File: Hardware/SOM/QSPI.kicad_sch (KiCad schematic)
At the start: 1 part, among them U4 W25Q128JVP

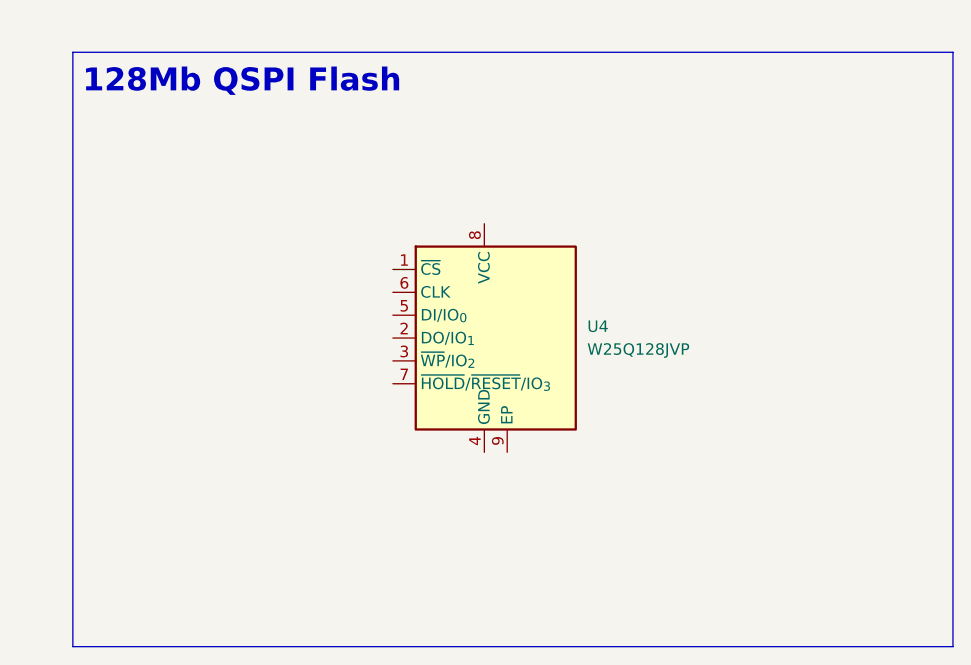
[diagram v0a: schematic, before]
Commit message: QSPI, banks IO decoupling
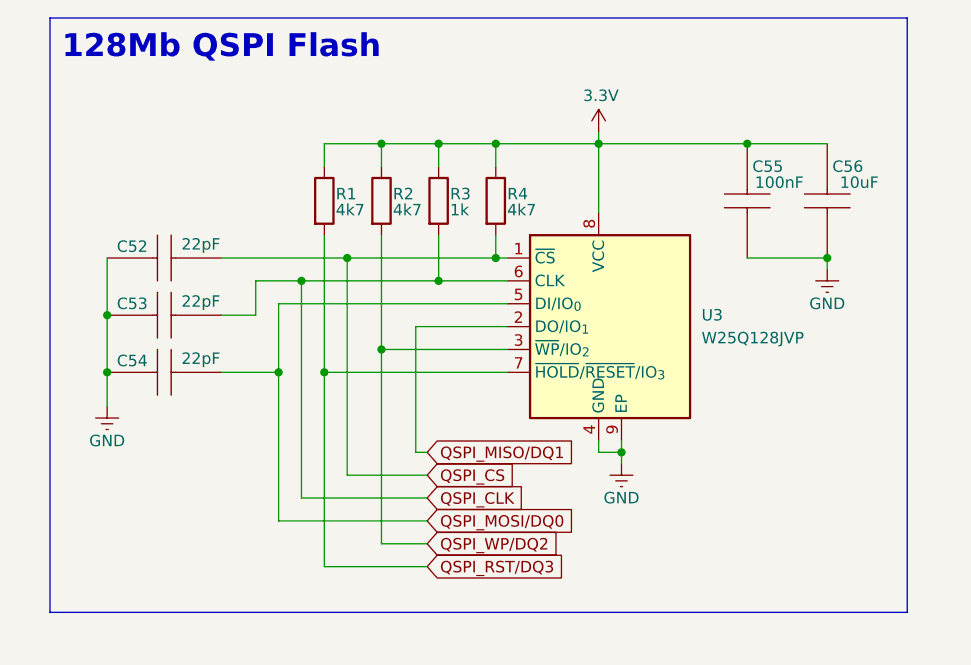
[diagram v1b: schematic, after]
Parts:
- added C52, C53, C54: 22pF, Capacitor_SMD:C_0402_1005Metric, symbol RA8M1:885012205092
- added C55: 100nF, Capacitor_SMD:C_0402_1005Metric, symbol RA8M1:885012205092
- added C56: 10uF, Capacitor_SMD:C_0402_1005Metric, symbol RA8M1:885012205092
- added R1, R2, R4: 4k7, Resistor_SMD:R_0402_1005Metric, symbol Device:R
- added R3: 1k, Resistor_SMD:R_0402_1005Metric, symbol Device:R
- renumbered U4 to U3
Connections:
- net QSPI_CS: now reaches U3.1 (~{CS})
- net QSPI_CS: now also C52.1, R4.2
- net QSPI_MISO/DQ1: now reaches U3.2 (DO/IO_{1})
- net QSPI_WP/DQ2: now reaches U3.3 (~{WP}/IO_{2})
- net QSPI_WP/DQ2: now also R2.2
- net GND: now reaches U3.4 (GND)
- net GND: now also U3.9 (EP), C52.2, C53.2, C54.2, C55.1, C56.1
- net QSPI_MOSI/DQ0: now reaches U3.5 (DI/IO_{0})
- net QSPI_MOSI/DQ0: now also C54.1
- net QSPI_CLK: now reaches U3.6 (CLK)
- net QSPI_CLK: now also C53.1, R3.2
- net QSPI_RST/DQ3: now reaches U3.7 (~{HOLD}/~{RESET}/IO_{3})
- net QSPI_RST/DQ3: now also R1.2
- net 3.3V: now reaches U3.8 (VCC)
- net 3.3V: now also C55.2, C56.2, R1.1, R2.1, R3.1, R4.1
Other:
- moved on the sheet: U3

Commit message: QSPI connected
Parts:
- added R5: 0R, Resistor_SMD:R_0402_1005Metric, symbol Device:R
- added R6: 49.9R, Resistor_SMD:R_0402_1005Metric, symbol Device:R
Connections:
- net QSPI_CLK: now also R6.2; no longer C53.1, R3.2, U3.6 (CLK)
- net QSPI_CS: now also R5.2; no longer C52.1, R4.2, U3.1 (~{CS})
- new net: C53.1, R3.2, R6.1, U3.6 (CLK)
- new net: C52.1, R4.2, R5.1, U3.1 (~{CS})
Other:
- moved on the sheet: C52, C53, C54

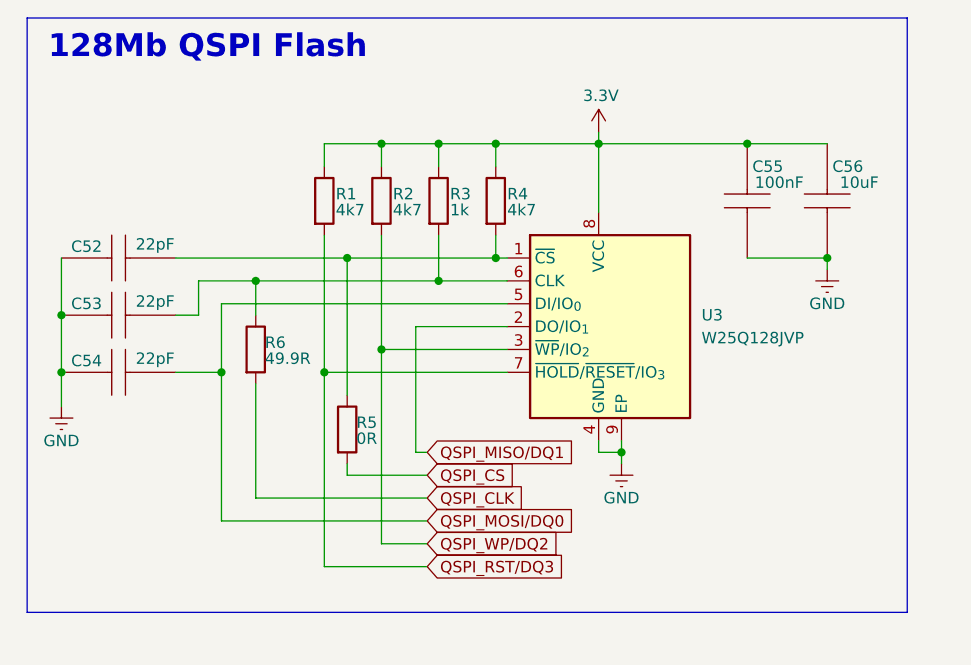
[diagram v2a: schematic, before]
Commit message: SOM: DDR pull-ups
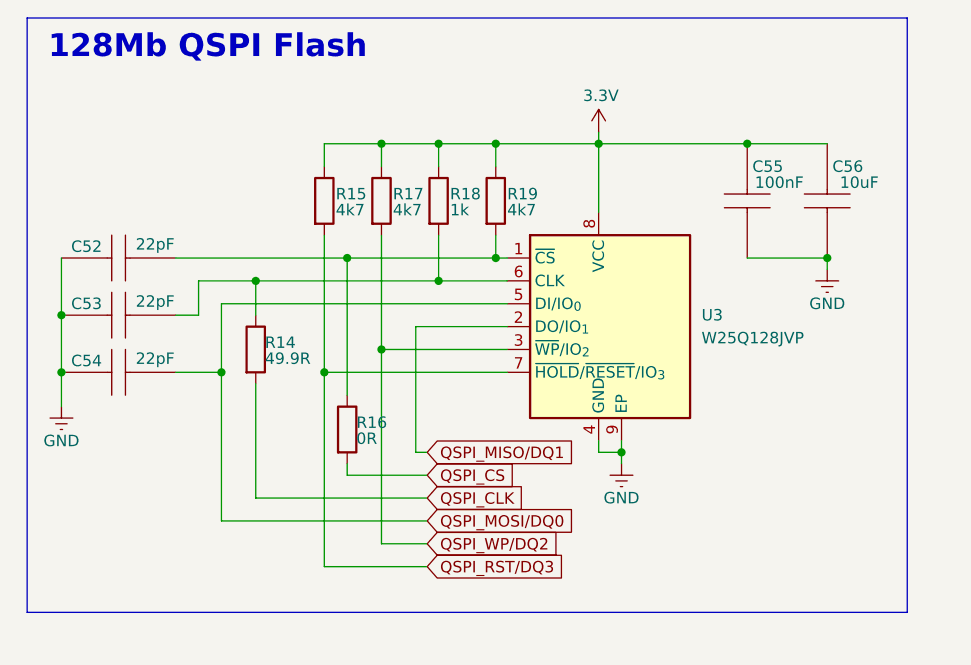
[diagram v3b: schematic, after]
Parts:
- renumbered R6 to R14, R1 to R15, R5 to R16, R2 to R17, R3 to R18, R4 to R19
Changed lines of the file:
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@@
 		(on_board yes)
 		(dnp no)
-		(property "Reference" "R2"
+		(property "Reference" "R17"
 			(at 137.16 84.328 0)
 			(effects
@@
 			(project "LFE5UM5G-85F_SOM"
 				(path "/de32abb0-ff3b-4c67-a91a-eed08140b1b2/2798ff7a-264e-45e9-a081-6e03072ed147"
-					(reference "R2")
+					(reference "R17")
 					(unit 1)
 				)
@@
 		(on_board yes)
 		(dnp no)
-		(property "Reference" "R6"
+		(property "Reference" "R14"
 			(at 122.936 100.838 0)
 			(effects
@@
 			(project "LFE5UM5G-85F_SOM"
 				(path "/de32abb0-ff3b-4c67-a91a-eed08140b1b2/2798ff7a-264e-45e9-a081-6e03072ed147"
-					(reference "R6")
+					(reference "R14")
 					(unit 1)
 				)
@@
 		(on_board yes)
 		(dnp no)
-		(property "Reference" "#PWR031"
+		(property "Reference" "#PWR038"
 			(at 160.02 81.28 0)
 			(effects
@@
 			(project "LFE5UM5G-85F_SOM"
 				(path "/de32abb0-ff3b-4c67-a91a-eed08140b1b2/2798ff7a-264e-45e9-a081-6e03072ed147"
-					(reference "#PWR031")
+					(reference "#PWR038")
 					(unit 1)
 				)
@@
 		(on_board yes)
 		(dnp no)
-		(property "Reference" "R5"
+		(property "Reference" "R16"
 			(at 133.096 109.728 0)
 			(effects
@@
 			(project "LFE5UM5G-85F_SOM"
 				(path "/de32abb0-ff3b-4c67-a91a-eed08140b1b2/2798ff7a-264e-45e9-a081-6e03072ed147"
-					(reference "R5")
+					(reference "R16")
 					(unit 1)
 				)
@@
 		(on_board yes)
 		(dnp no)
-		(property "Reference" "#PWR030"
+		(property "Reference" "#PWR037"
 			(at 100.33 114.3 0)
 			(effects
@@
 			(project "LFE5UM5G-85F_SOM"
 				(path "/de32abb0-ff3b-4c67-a91a-eed08140b1b2/2798ff7a-264e-45e9-a081-6e03072ed147"
-					(reference "#PWR030")
+					(reference "#PWR037")
 					(unit 1)
 				)
@@
 		(on_board yes)
 		(dnp no)
-		(property "Reference" "R1"
+		(property "Reference" "R15"
 			(at 130.81 84.328 0)
 			(effects
@@
 			(project "LFE5UM5G-85F_SOM"
 				(path "/de32abb0-ff3b-4c67-a91a-eed08140b1b2/2798ff7a-264e-45e9-a081-6e03072ed147"
-					(reference "R1")
+					(reference "R15")
 					(unit 1)
 				)
@@
 		(on_board yes)
 		(dnp no)
-		(property "Reference" "#PWR032"
+		(property "Reference" "#PWR039"
 			(at 162.56 120.65 0)
 			(effects
@@
 			(project "LFE5UM5G-85F_SOM"
 				(path "/de32abb0-ff3b-4c67-a91a-eed08140b1b2/2798ff7a-264e-45e9-a081-6e03072ed147"
-					(reference "#PWR032")
+					(reference "#PWR039")
 					(unit 1)
 				)
@@
 		(on_board yes)
 		(dnp no)
-		(property "Reference" "R3"
+		(property "Reference" "R18"
 			(at 143.51 84.328 0)
 			(effects
@@
 			(project "LFE5UM5G-85F_SOM"
 				(path "/de32abb0-ff3b-4c67-a91a-eed08140b1b2/2798ff7a-264e-45e9-a081-6e03072ed147"
-					(reference "R3")
+					(reference "R18")
 					(unit 1)
 				)
@@
 		(on_board yes)
 		(dnp no)
-		(property "Reference" "#PWR033"
+		(property "Reference" "#PWR040"
 			(at 185.42 99.06 0)
 			(effects
@@
 			(project "LFE5UM5G-85F_SOM"
 				(path "/de32abb0-ff3b-4c67-a91a-eed08140b1b2/2798ff7a-264e-45e9-a081-6e03072ed147"
-					(reference "#PWR033")
+					(reference "#PWR040")
 					(unit 1)
 				)
@@
 		(on_board yes)
 		(dnp no)
-		(property "Reference" "R4"
+		(property "Reference" "R19"
 			(at 149.86 84.328 0)
 			(effects
@@
 			(project "LFE5UM5G-85F_SOM"
 				(path "/de32abb0-ff3b-4c67-a91a-eed08140b1b2/2798ff7a-264e-45e9-a081-6e03072ed147"
-					(reference "R4")
-					(unit 1)
-				)
+					(reference "R19")
+					(unit 1)
+				)

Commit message: SOM: power supply update
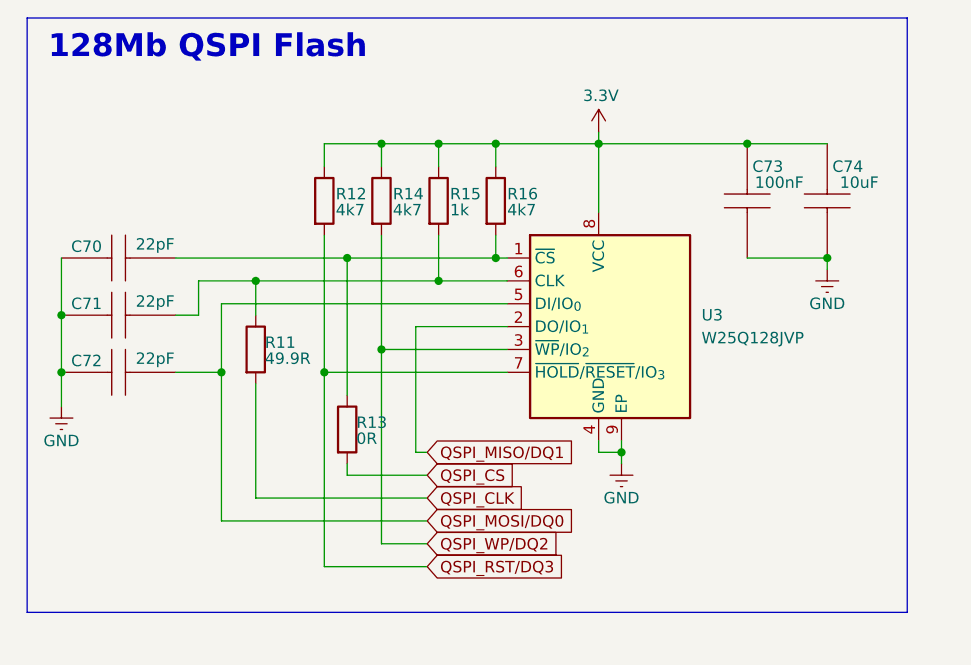
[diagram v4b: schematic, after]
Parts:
- renumbered C52 to C70, C53 to C71, C54 to C72, C55 to C73, C56 to C74, R14 to R11, R15 to R12, R16 to R13, R17 to R14, R18 to R15, R19 to R16
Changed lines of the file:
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@@
 		(on_board yes)
 		(dnp no)
-		(property "Reference" "R17"
+		(property "Reference" "R14"
 			(at 137.16 84.328 0)
 			(effects
@@
 			(project "LFE5UM5G-85F_SOM"
 				(path "/de32abb0-ff3b-4c67-a91a-eed08140b1b2/2798ff7a-264e-45e9-a081-6e03072ed147"
-					(reference "R17")
+					(reference "R14")
 					(unit 1)
 				)
@@
 		(on_board yes)
 		(dnp no)
-		(property "Reference" "R14"
+		(property "Reference" "R11"
 			(at 122.936 100.838 0)
 			(effects
@@
 			(project "LFE5UM5G-85F_SOM"
 				(path "/de32abb0-ff3b-4c67-a91a-eed08140b1b2/2798ff7a-264e-45e9-a081-6e03072ed147"
-					(reference "R14")
+					(reference "R11")
 					(unit 1)
 				)
@@
 		(on_board yes)
 		(dnp no)
-		(property "Reference" "#PWR038"
+		(property "Reference" "#PWR043"
 			(at 160.02 81.28 0)
 			(effects
@@
 			(project "LFE5UM5G-85F_SOM"
 				(path "/de32abb0-ff3b-4c67-a91a-eed08140b1b2/2798ff7a-264e-45e9-a081-6e03072ed147"
-					(reference "#PWR038")
+					(reference "#PWR043")
 					(unit 1)
 				)
@@
 		(on_board yes)
 		(dnp no)
-		(property "Reference" "R16"
+		(property "Reference" "R13"
 			(at 133.096 109.728 0)
 			(effects
@@
 			(project "LFE5UM5G-85F_SOM"
 				(path "/de32abb0-ff3b-4c67-a91a-eed08140b1b2/2798ff7a-264e-45e9-a081-6e03072ed147"
-					(reference "R16")
+					(reference "R13")
 					(unit 1)
 				)
@@
 		(on_board yes)
 		(dnp no)
-		(property "Reference" "C52"
+		(property "Reference" "C70"
 			(at 103.124 90.17 0)
 			(effects
@@
 			(project "LFE5UM5G-85F_SOM"
 				(path "/de32abb0-ff3b-4c67-a91a-eed08140b1b2/2798ff7a-264e-45e9-a081-6e03072ed147"
-					(reference "C52")
+					(reference "C70")
 					(unit 1)
 				)
@@
 		(on_board yes)
 		(dnp no)
-		(property "Reference" "#PWR037"
+		(property "Reference" "#PWR042"
 			(at 100.33 114.3 0)
 			(effects
@@
 			(project "LFE5UM5G-85F_SOM"
 				(path "/de32abb0-ff3b-4c67-a91a-eed08140b1b2/2798ff7a-264e-45e9-a081-6e03072ed147"
-					(reference "#PWR037")
+					(reference "#PWR042")
 					(unit 1)
 				)
@@
 		(on_board yes)
 		(dnp no)
-		(property "Reference" "C55"
+		(property "Reference" "C73"
 			(at 178.816 81.28 90)
 			(effects
@@
 			(project "LFE5UM5G-85F_SOM"
 				(path "/de32abb0-ff3b-4c67-a91a-eed08140b1b2/2798ff7a-264e-45e9-a081-6e03072ed147"
-					(reference "C55")
+					(reference "C73")
 					(unit 1)
 				)
@@
 		(on_board yes)
 		(dnp no)
-		(property "Reference" "C53"
+		(property "Reference" "C71"
 			(at 103.124 96.52 0)
 			(effects
@@
 			(project "LFE5UM5G-85F_SOM"
 				(path "/de32abb0-ff3b-4c67-a91a-eed08140b1b2/2798ff7a-264e-45e9-a081-6e03072ed147"
-					(reference "C53")
+					(reference "C71")
 					(unit 1)
 				)
@@
 		(on_board yes)
 		(dnp no)
-		(property "Reference" "C56"
+		(property "Reference" "C74"
 			(at 187.706 81.28 90)
 			(effects
@@
 			(project "LFE5UM5G-85F_SOM"
 				(path "/de32abb0-ff3b-4c67-a91a-eed08140b1b2/2798ff7a-264e-45e9-a081-6e03072ed147"
-					(reference "C56")
+					(reference "C74")
 					(unit 1)
 				)
@@
 		(on_board yes)
 		(dnp no)
-		(property "Reference" "R15"
+		(property "Reference" "R12"
 			(at 130.81 84.328 0)
 			(effects
@@
 			(project "LFE5UM5G-85F_SOM"
 				(path "/de32abb0-ff3b-4c67-a91a-eed08140b1b2/2798ff7a-264e-45e9-a081-6e03072ed147"
-					(reference "R15")
+					(reference "R12")
 					(unit 1)
 				)
@@
 		(on_board yes)
 		(dnp no)
-		(property "Reference" "#PWR039"
+		(property "Reference" "#PWR044"
 			(at 162.56 120.65 0)
 			(effects
@@
 			(project "LFE5UM5G-85F_SOM"
 				(path "/de32abb0-ff3b-4c67-a91a-eed08140b1b2/2798ff7a-264e-45e9-a081-6e03072ed147"
-					(reference "#PWR039")
+					(reference "#PWR044")
 					(unit 1)
 				)
@@
 		(on_board yes)
 		(dnp no)
-		(property "Reference" "C54"
+		(property "Reference" "C72"
 			(at 103.124 102.87 0)
 			(effects
@@
 			(project "LFE5UM5G-85F_SOM"
 				(path "/de32abb0-ff3b-4c67-a91a-eed08140b1b2/2798ff7a-264e-45e9-a081-6e03072ed147"
-					(reference "C54")
+					(reference "C72")
 					(unit 1)
 				)
@@
 		(on_board yes)
 		(dnp no)
-		(property "Reference" "R18"
+		(property "Reference" "R15"
 			(at 143.51 84.328 0)
 			(effects
@@
 			(project "LFE5UM5G-85F_SOM"
 				(path "/de32abb0-ff3b-4c67-a91a-eed08140b1b2/2798ff7a-264e-45e9-a081-6e03072ed147"
-					(reference "R18")
+					(reference "R15")
 					(unit 1)
 				)
@@
 		(on_board yes)
 		(dnp no)
-		(property "Reference" "#PWR040"
+		(property "Reference" "#PWR045"
 			(at 185.42 99.06 0)
 			(effects
@@
 			(project "LFE5UM5G-85F_SOM"
 				(path "/de32abb0-ff3b-4c67-a91a-eed08140b1b2/2798ff7a-264e-45e9-a081-6e03072ed147"
-					(reference "#PWR040")
+					(reference "#PWR045")
 					(unit 1)
 				)
@@
 		(on_board yes)
 		(dnp no)
-		(property "Reference" "R19"
+		(property "Reference" "R16"
 			(at 149.86 84.328 0)
 			(effects
@@
 			(project "LFE5UM5G-85F_SOM"
 				(path "/de32abb0-ff3b-4c67-a91a-eed08140b1b2/2798ff7a-264e-45e9-a081-6e03072ed147"
-					(reference "R19")
-					(unit 1)
-				)
+					(reference "R16")
+					(unit 1)
+				)

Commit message: SOM: layout update
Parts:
- renumbered C70 to C90, C71 to C91, C72 to C92, C73 to C93, C74 to C94
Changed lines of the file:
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@@
 		(on_board yes)
 		(dnp no)
-		(property "Reference" "#PWR043"
+		(property "Reference" "#PWR070"
 			(at 160.02 81.28 0)
 			(effects
@@
 			(project "LFE5UM5G-85F_SOM"
 				(path "/de32abb0-ff3b-4c67-a91a-eed08140b1b2/2798ff7a-264e-45e9-a081-6e03072ed147"
-					(reference "#PWR043")
+					(reference "#PWR070")
 					(unit 1)
 				)
@@
 		(on_board yes)
 		(dnp no)
-		(property "Reference" "C70"
+		(property "Reference" "C90"
 			(at 103.124 90.17 0)
 			(effects
@@
 			(project "LFE5UM5G-85F_SOM"
 				(path "/de32abb0-ff3b-4c67-a91a-eed08140b1b2/2798ff7a-264e-45e9-a081-6e03072ed147"
-					(reference "C70")
+					(reference "C90")
 					(unit 1)
 				)
@@
 		(on_board yes)
 		(dnp no)
-		(property "Reference" "#PWR042"
+		(property "Reference" "#PWR069"
 			(at 100.33 114.3 0)
 			(effects
@@
 			(project "LFE5UM5G-85F_SOM"
 				(path "/de32abb0-ff3b-4c67-a91a-eed08140b1b2/2798ff7a-264e-45e9-a081-6e03072ed147"
-					(reference "#PWR042")
+					(reference "#PWR069")
 					(unit 1)
 				)
@@
 		(on_board yes)
 		(dnp no)
-		(property "Reference" "C73"
+		(property "Reference" "C93"
 			(at 178.816 81.28 90)
 			(effects
@@
 			(project "LFE5UM5G-85F_SOM"
 				(path "/de32abb0-ff3b-4c67-a91a-eed08140b1b2/2798ff7a-264e-45e9-a081-6e03072ed147"
-					(reference "C73")
+					(reference "C93")
 					(unit 1)
 				)
@@
 		(on_board yes)
 		(dnp no)
-		(property "Reference" "C71"
+		(property "Reference" "C91"
 			(at 103.124 96.52 0)
 			(effects
@@
 			(project "LFE5UM5G-85F_SOM"
 				(path "/de32abb0-ff3b-4c67-a91a-eed08140b1b2/2798ff7a-264e-45e9-a081-6e03072ed147"
-					(reference "C71")
+					(reference "C91")
 					(unit 1)
 				)
@@
 		(on_board yes)
 		(dnp no)
-		(property "Reference" "C74"
+		(property "Reference" "C94"
 			(at 187.706 81.28 90)
 			(effects
@@
 			(project "LFE5UM5G-85F_SOM"
 				(path "/de32abb0-ff3b-4c67-a91a-eed08140b1b2/2798ff7a-264e-45e9-a081-6e03072ed147"
-					(reference "C74")
+					(reference "C94")
 					(unit 1)
 				)
@@
 		(on_board yes)
 		(dnp no)
-		(property "Reference" "#PWR044"
+		(property "Reference" "#PWR071"
 			(at 162.56 120.65 0)
 			(effects
@@
 			(project "LFE5UM5G-85F_SOM"
 				(path "/de32abb0-ff3b-4c67-a91a-eed08140b1b2/2798ff7a-264e-45e9-a081-6e03072ed147"
-					(reference "#PWR044")
+					(reference "#PWR071")
 					(unit 1)
 				)
@@
 		(on_board yes)
 		(dnp no)
-		(property "Reference" "C72"
+		(property "Reference" "C92"
 			(at 103.124 102.87 0)
 			(effects
@@
 			(project "LFE5UM5G-85F_SOM"
 				(path "/de32abb0-ff3b-4c67-a91a-eed08140b1b2/2798ff7a-264e-45e9-a081-6e03072ed147"
-					(reference "C72")
+					(reference "C92")
 					(unit 1)
 				)
@@
 		(on_board yes)
 		(dnp no)
-		(property "Reference" "#PWR045"
+		(property "Reference" "#PWR072"
 			(at 185.42 99.06 0)
 			(effects
@@
 			(project "LFE5UM5G-85F_SOM"
 				(path "/de32abb0-ff3b-4c67-a91a-eed08140b1b2/2798ff7a-264e-45e9-a081-6e03072ed147"
-					(reference "#PWR045")
-					(unit 1)
-				)
+					(reference "#PWR072")
+					(unit 1)
+				)
